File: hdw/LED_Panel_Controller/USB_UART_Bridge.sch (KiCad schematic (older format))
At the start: 46 parts, among them J1501 USB_B_Mini, U1501 74LVC1G97, U1502 CP2105, U1503 TXB0104RGY, U1504 TPD3S014DBVR

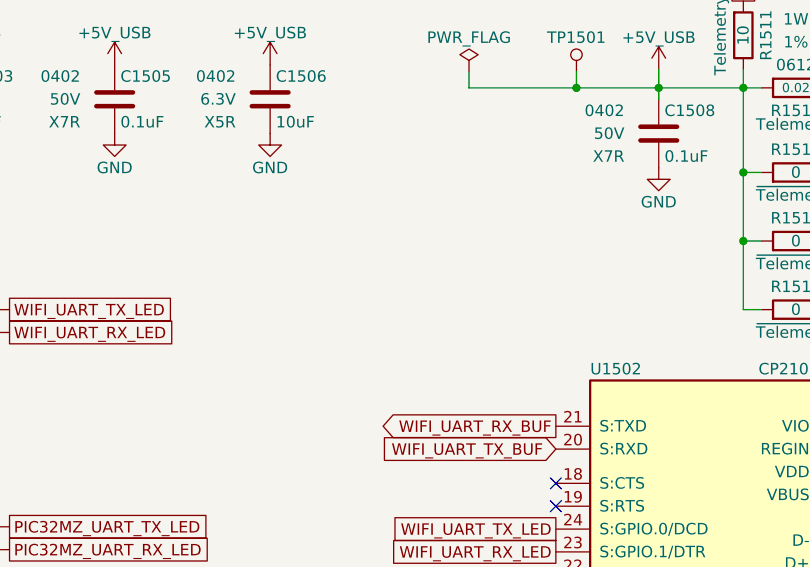
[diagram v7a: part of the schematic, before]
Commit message: ran erc, annotated schematic, added hardstraps to MCU
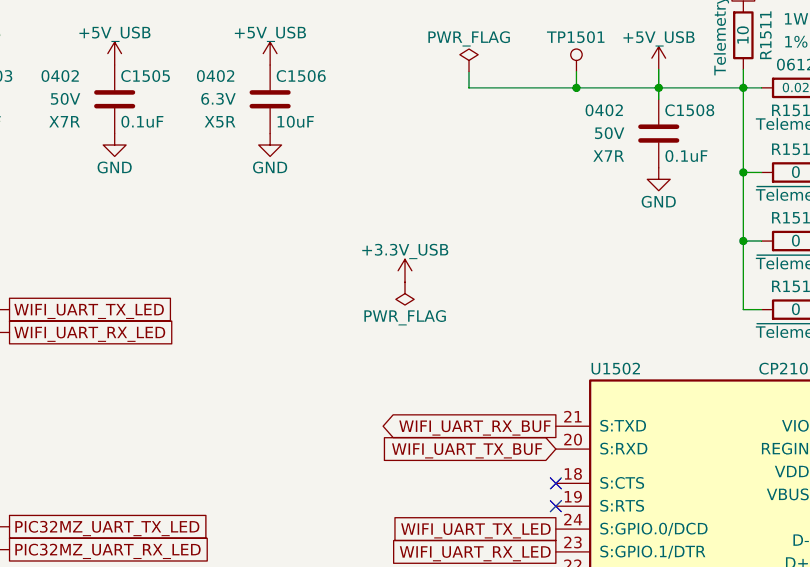
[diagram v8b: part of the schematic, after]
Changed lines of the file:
@@
 $EndComp
 $Comp
-L power:PWR_FLAG #FLG01502
+L power:PWR_FLAG #FLG01503
 U 1 1 5BB10D97
 P 7360 3290
-F 0 "#FLG01502" H 7360 3365 50  0001 C CNN
+F 0 "#FLG01503" H 7360 3365 50  0001 C CNN
 F 1 "PWR_FLAG" V 7360 3440 50  0000 L CNN
 F 2 "" H 7360 3290 50  0001 C CNN
@@
 POS5_USB_PGOOD
 $Comp
-L power:GND #PWR01535
+L power:GND #PWR01536
 U 1 1 5E9AEFB8
 P 6590 3690
-F 0 "#PWR01535" H 6590 3440 50  0001 C CNN
+F 0 "#PWR01536" H 6590 3440 50  0001 C CNN
 F 1 "GND" H 6590 3540 50  0000 C CNN
 F 2 "" H 6590 3690 50  0001 C CNN
@@
 $EndComp
 $Comp
-L power:GND #PWR01523
+L power:GND #PWR01524
 U 1 1 5E9AF283
 P 4740 3640
-F 0 "#PWR01523" H 4740 3390 50  0001 C CNN
+F 0 "#PWR01524" H 4740 3390 50  0001 C CNN
 F 1 "GND" H 4740 3490 50  0000 C CNN
 F 2 "" H 4740 3640 50  0001 C CNN
@@
 	3910 3220 3910 3290
 $Comp
-L power:PWR_FLAG #FLG01501
+L power:PWR_FLAG #FLG01502
 U 1 1 5E475BF2
 P 3910 3220
-F 0 "#FLG01501" H 3910 3295 50  0001 C CNN
+F 0 "#FLG01502" H 3910 3295 50  0001 C CNN
 F 1 "PWR_FLAG" H 3910 3370 50  0000 C CNN
 F 2 "" H 3910 3220 50  0001 C CNN
@@
 	4740 3210 4740 3290
 $Comp
-L Custom_Library:+5V_USB #PWR01522
+L Custom_Library:+5V_USB #PWR01523
 U 1 1 5BBEEF4D
 P 4740 3210
-F 0 "#PWR01522" H 4740 3060 50  0001 C CNN
+F 0 "#PWR01523" H 4740 3060 50  0001 C CNN
 F 1 "+5V_USB" H 4740 3350 50  0000 C CNN
 F 2 "" H 4740 3210 50  0001 C CNN
@@
 $EndComp
 $Comp
-L Custom_Library:+3.3V_USB #PWR01533
+L Custom_Library:+3.3V_USB #PWR01534
 U 1 1 5F3A38A3
 P 6520 950
-F 0 "#PWR01533" H 6520 800 50  0001 C CNN
+F 0 "#PWR01534" H 6520 800 50  0001 C CNN
 F 1 "+3.3V_USB" H 6650 1090 50  0000 C CNN
 F 2 "" H 6520 950 50  0001 C CNN
@@
 $EndComp
 $Comp
-L power:+3.3V #PWR01531
+L power:+3.3V #PWR01532
 U 1 1 5F3A3F67
 P 6320 950
-F 0 "#PWR01531" H 6320 800 50  0001 C CNN
+F 0 "#PWR01532" H 6320 800 50  0001 C CNN
 F 1 "+3.3V" H 6270 1090 50  0000 C CNN
 F 2 "" H 6320 950 50  0001 C CNN
@@
 $EndComp
 $Comp
-L power:GND #PWR01534
+L power:GND #PWR01535
 U 1 1 5F3A6750
 P 6520 2350
-F 0 "#PWR01534" H 6520 2100 50  0001 C CNN
+F 0 "#PWR01535" H 6520 2100 50  0001 C CNN
 F 1 "GND" H 6520 2200 50  0000 C CNN
 F 2 "" H 6520 2350 50  0001 C CNN
@@
 PIC32MZ_UART_TX_BUF
 $Comp
-L Custom_Library:+3.3V_USB #PWR01538
+L Custom_Library:+3.3V_USB #PWR01539
 U 1 1 5F3B0FEC
 P 7290 970
-F 0 "#PWR01538" H 7290 820 50  0001 C CNN
+F 0 "#PWR01539" H 7290 820 50  0001 C CNN
 F 1 "+3.3V_USB" H 7290 1110 50  0000 C CNN
 F 2 "" H 7290 970 50  0001 C CNN
@@
 $EndComp
 $Comp
-L Custom_Library:+3.3V_USB #PWR01539
+L Custom_Library:+3.3V_USB #PWR01540
 U 1 1 5F3B149F
 P 7790 970
-F 0 "#PWR01539" H 7790 820 50  0001 C CNN
+F 0 "#PWR01540" H 7790 820 50  0001 C CNN
 F 1 "+3.3V_USB" H 7790 1110 50  0000 C CNN
 F 2 "" H 7790 970 50  0001 C CNN
@@
 $EndComp
 $Comp
-L power:GND #PWR01537
+L power:GND #PWR01538
 U 1 1 5F3FC0EC
 P 7180 2710
-F 0 "#PWR01537" H 7180 2460 50  0001 C CNN
+F 0 "#PWR01538" H 7180 2460 50  0001 C CNN
 F 1 "GND" H 7180 2560 50  0000 C CNN
 F 2 "" H 7180 2710 50  0001 C CNN
@@
 $EndComp
 $Comp
-L power:GND #PWR01541
+L power:GND #PWR01542
 U 1 1 5F40283B
 P 7890 2710
-F 0 "#PWR01541" H 7890 2460 50  0001 C CNN
+F 0 "#PWR01542" H 7890 2460 50  0001 C CNN
 F 1 "GND" H 7890 2560 50  0000 C CNN
 F 2 "" H 7890 2710 50  0001 C CNN
@@
 $EndComp
 $Comp
-L Custom_Library:+3.3V_USB #PWR01540
+L Custom_Library:+3.3V_USB #PWR01541
 U 1 1 5F402845
 P 7890 2410
-F 0 "#PWR01540" H 7890 2260 50  0001 C CNN
+F 0 "#PWR01541" H 7890 2260 50  0001 C CNN
 F 1 "+3.3V_USB" H 7890 2550 50  0000 C CNN
 F 2 "" H 7890 2410 50  0001 C CNN
@@
 $EndComp
 $Comp
-L power:+3.3V #PWR01536
+L power:+3.3V #PWR01537
 U 1 1 5F405693
 P 7180 2410
-F 0 "#PWR01536" H 7180 2260 50  0001 C CNN
+F 0 "#PWR01537" H 7180 2260 50  0001 C CNN
 F 1 "+3.3V" H 7180 2550 50  0000 C CNN
 F 2 "" H 7180 2410 50  0001 C CNN
@@
 $EndComp
 $Comp
-L power:GND #PWR01529
+L power:GND #PWR01530
 U 1 1 5F7F50BE
 P 5670 6550
-F 0 "#PWR01529" H 5670 6300 50  0001 C CNN
+F 0 "#PWR01530" H 5670 6300 50  0001 C CNN
 F 1 "GND" H 5670 6400 50  0000 C CNN
 F 2 "" H 5670 6550 50  0001 C CNN
@@
 	5590 5370 6840 5370
 $Comp
-L Custom_Library:+3.3V_USB #PWR01527
+L Custom_Library:+3.3V_USB #PWR01528
 U 1 1 5F80B61B
 P 5590 4970
-F 0 "#PWR01527" H 5590 4820 50  0001 C CNN
+F 0 "#PWR01528" H 5590 4820 50  0001 C CNN
 F 1 "+3.3V_USB" V 5590 5110 50  0000 L CNN
 F 2 "" H 5590 4970 50  0001 C CNN
@@
 $EndComp
 $Comp
-L Custom_Library:+3.3V_USB #PWR01525
+L Custom_Library:+3.3V_USB #PWR01526
 U 1 1 5F80D319
 P 5590 4770
-F 0 "#PWR01525" H 5590 4620 50  0001 C CNN
+F 0 "#PWR01526" H 5590 4620 50  0001 C CNN
 F 1 "+3.3V_USB" V 5590 4910 50  0000 L CNN
 F 2 "" H 5590 4770 50  0001 C CNN
@@
 $EndComp
 $Comp
-L Custom_Library:+5V_USB #PWR01528
+L Custom_Library:+5V_USB #PWR01529
 U 1 1 5F80EDF3
 P 5590 5070
-F 0 "#PWR01528" H 5590 4920 50  0001 C CNN
+F 0 "#PWR01529" H 5590 4920 50  0001 C CNN
 F 1 "+5V_USB" V 5590 5210 50  0000 L CNN
 F 2 "" H 5590 5070 50  0001 C CNN
@@
 $EndComp
 $Comp
-L Custom_Library:+5V_USB #PWR01526
+L Custom_Library:+5V_USB #PWR01527
 U 1 1 5F80F76A
 P 5590 4870
-F 0 "#PWR01526" H 5590 4720 50  0001 C CNN
+F 0 "#PWR01527" H 5590 4720 50  0001 C CNN
 F 1 "+5V_USB" V 5590 5010 50  0000 L CNN
 F 2 "" H 5590 4870 50  0001 C CNN
@@
 $EndComp
 $Comp
-L Custom_Library:+3.3V_USB #PWR01530
+L Custom_Library:+3.3V_USB #PWR01531
 U 1 1 5F8198B9
 P 5890 5670
-F 0 "#PWR01530" H 5890 5520 50  0001 C CNN
+F 0 "#PWR01531" H 5890 5520 50  0001 C CNN
 F 1 "+3.3V_USB" V 5890 5810 50  0000 L CNN
 F 2 "" H 5890 5670 50  0001 C CNN
@@
 NoConn ~ 8550 5470
 $Comp
-L power:GND #PWR01544
+L power:GND #PWR01545
 U 1 1 5F7CA170
 P 8850 5670
-F 0 "#PWR01544" H 8850 5420 50  0001 C CNN
+F 0 "#PWR01545" H 8850 5420 50  0001 C CNN
 F 1 "GND" H 8850 5520 50  0000 C CNN
 F 2 "" H 8850 5670 50  0001 C CNN
@@
 	8950 5930 8950 5670
 $Comp
-L power:GND #PWR01545
+L power:GND #PWR01546
 U 1 1 5F7CB802
 P 8950 6230
-F 0 "#PWR01545" H 8950 5980 50  0001 C CNN
+F 0 "#PWR01546" H 8950 5980 50  0001 C CNN
 F 1 "GND" H 8950 6080 50  0000 C CNN
 F 2 "" H 8950 6230 50  0001 C CNN
@@
 $EndComp
 $Comp
-L power:GND #PWR01520
+L power:GND #PWR01521
 U 1 1 5F7D8449
 P 4210 6910
-F 0 "#PWR01520" H 4210 6660 50  0001 C CNN
+F 0 "#PWR01521" H 4210 6660 50  0001 C CNN
 F 1 "GND" H 4210 6760 50  0000 C CNN
 F 2 "" H 4210 6910 50  0001 C CNN
@@
 $EndComp
 $Comp
-L power:GND #PWR01532
+L power:GND #PWR01533
 U 1 1 5F8020F2
 P 6320 2350
-F 0 "#PWR01532" H 6320 2100 50  0001 C CNN
+F 0 "#PWR01533" H 6320 2100 50  0001 C CNN
 F 1 "GND" H 6320 2200 50  0000 C CNN
 F 2 "" H 6320 2350 50  0001 C CNN
@@
 	6820 1950 8790 1950
 $Comp
-L Custom_Library:+3.3V_USB #PWR01542
+L Custom_Library:+3.3V_USB #PWR01543
 U 1 1 5F819B78
 P 8290 970
-F 0 "#PWR01542" H 8290 820 50  0001 C CNN
+F 0 "#PWR01543" H 8290 820 50  0001 C CNN
 F 1 "+3.3V_USB" H 8290 1110 50  0000 C CNN
 F 2 "" H 8290 970 50  0001 C CNN
@@
 $EndComp
 $Comp
-L Custom_Library:+3.3V_USB #PWR01543
+L Custom_Library:+3.3V_USB #PWR01544
 U 1 1 5F819DB3
 P 8790 970
-F 0 "#PWR01543" H 8790 820 50  0001 C CNN
+F 0 "#PWR01544" H 8790 820 50  0001 C CNN
 F 1 "+3.3V_USB" H 8790 1110 50  0000 C CNN
 F 2 "" H 8790 970 50  0001 C CNN
@@
 $EndComp
 $Comp
-L power:+3.3V #PWR01524
+L power:+3.3V #PWR01525
 U 1 1 6028B0DB
 P 4990 970
-F 0 "#PWR01524" H 4990 820 50  0001 C CNN
+F 0 "#PWR01525" H 4990 820 50  0001 C CNN
 F 1 "+3.3V" H 4990 1110 50  0000 C CNN
 F 2 "" H 4990 970 50  0001 C CNN
@@
 $EndComp
 $Comp
-L power:+3.3V #PWR01521
+L power:+3.3V #PWR01522
 U 1 1 6028B7E3
 P 4490 970
-F 0 "#PWR01521" H 4490 820 50  0001 C CNN
+F 0 "#PWR01522" H 4490 820 50  0001 C CNN
 F 1 "+3.3V" H 4490 1110 50  0000 C CNN
 F 2 "" H 4490 970 50  0001 C CNN
@@
 $EndComp
 $Comp
-L power:+3.3V #PWR01519
+L power:+3.3V #PWR01520
 U 1 1 6028BBC0
 P 3990 970
-F 0 "#PWR01519" H 3990 820 50  0001 C CNN
+F 0 "#PWR01520" H 3990 820 50  0001 C CNN
 F 1 "+3.3V" H 3990 1110 50  0000 C CNN
 F 2 "" H 3990 970 50  0001 C CNN
@@
 Wire Wire Line
 	1170 7240 1170 7160
+$Comp
+L Custom_Library:+3.3V_USB #PWR01519
+U 1 1 607A887A
+P 3630 4140
+F 0 "#PWR01519" H 3630 3990 50  0001 C CNN
+F 1 "+3.3V_USB" H 3630 4280 50  0000 C CNN
+F 2 "" H 3630 4140 50  0001 C CNN
+F 3 "" H 3630 4140 50  0001 C CNN
+	1    3630 4140
+	1    0    0    -1
+$EndComp
+$Comp
+L power:PWR_FLAG #FLG01501
+U 1 1 607A8B3A
+P 3630 4140
+F 0 "#FLG01501" H 3630 4215 50  0001 C CNN
+F 1 "PWR_FLAG" H 3630 4290 50  0000 C CNN
+F 2 "" H 3630 4140 50  0001 C CNN
+F 3 "~" H 3630 4140 50  0001 C CNN
+	1    3630 4140
+	-1   0    0    1
+$EndComp
 $EndSCHEMATC
